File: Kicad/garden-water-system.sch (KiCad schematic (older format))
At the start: 30 parts, among them J1 Conn_01x02, J10 Screw_Terminal_01x05, J11 Conn_01x04, J12 Conn_01x05, J13 Jack-DC, J2 Conn_01x05, J3 Conn_01x03, J4 Conn_01x03, J5 Conn_01x03, J6 Conn_01x03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

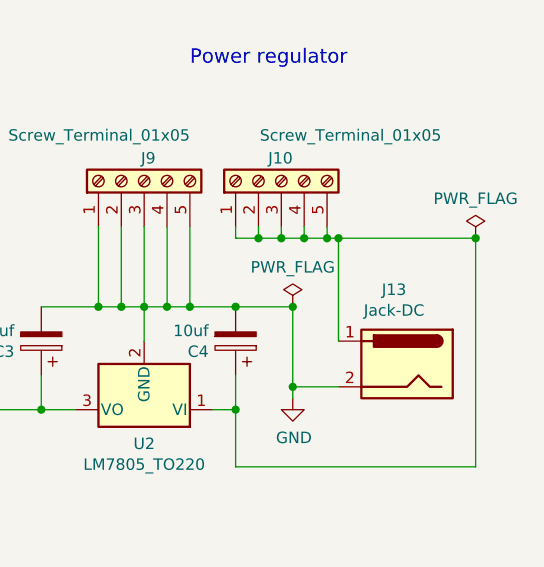
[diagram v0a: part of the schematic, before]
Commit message: Add protection diode on hardware power supply
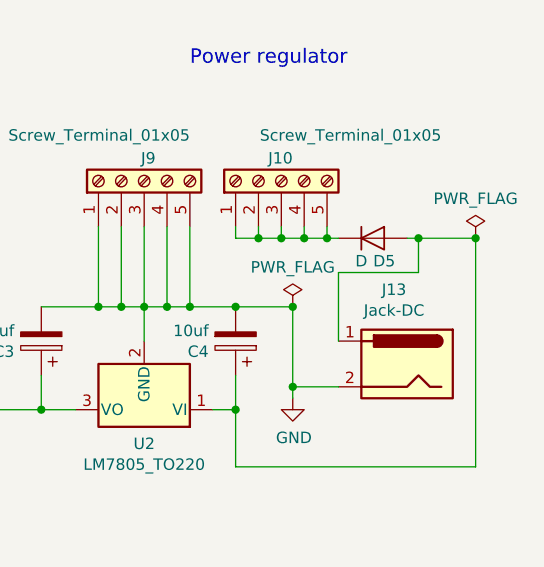
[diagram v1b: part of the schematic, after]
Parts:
- added D5: D, Diode_SMD:D_2010_5025Metric_Pad1.52x2.65mm_HandSolder, symbol Device:D
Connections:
- net at J10.1 (Pin_1), J10.2 (Pin_2), J10.3 (Pin_3)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: now also D5.1 (K); no longer C4.1, J13.1, U2.1 (VI)
- new net: C4.1, D5.2 (A), J13.1, U2.1 (VI)
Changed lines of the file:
@@
 	9400 2250 9400 2100
-Wire Wire Line
-	10200 1800 10250 1800
 Wire Wire Line
 	10850 1800 10850 2800
@@
 	9800 2800 10850 2800
 Wire Wire Line
-	10250 2250 10250 1800
-Connection ~ 10250 1800
-Wire Wire Line
-	10250 1800 10850 1800
+	10200 1800 10250 1800
+$Comp
+L Device:D D5
+U 1 1 5DFEEEC4
+P 10400 1800
+F 0 "D5" H 10450 1700 50  0000 C CNN
+F 1 "D" H 10350 1700 50  0000 C CNN
+F 2 "Diode_SMD:D_2010_5025Metric_Pad1.52x2.65mm_HandSolder" H 10400 1800 50  0001 C CNN
+F 3 "~" H 10400 1800 50  0001 C CNN
+	1    10400 1800
+	1    0    0    -1
+$EndComp
+Wire Wire Line
+	10550 1800 10600 1800
+Wire Wire Line
+	10250 2250 10250 1950
+Wire Wire Line
+	10250 1950 10600 1950
+Wire Wire Line
+	10600 1950 10600 1800
+Connection ~ 10600 1800
+Wire Wire Line
+	10600 1800 10850 1800
 $EndSCHEMATC

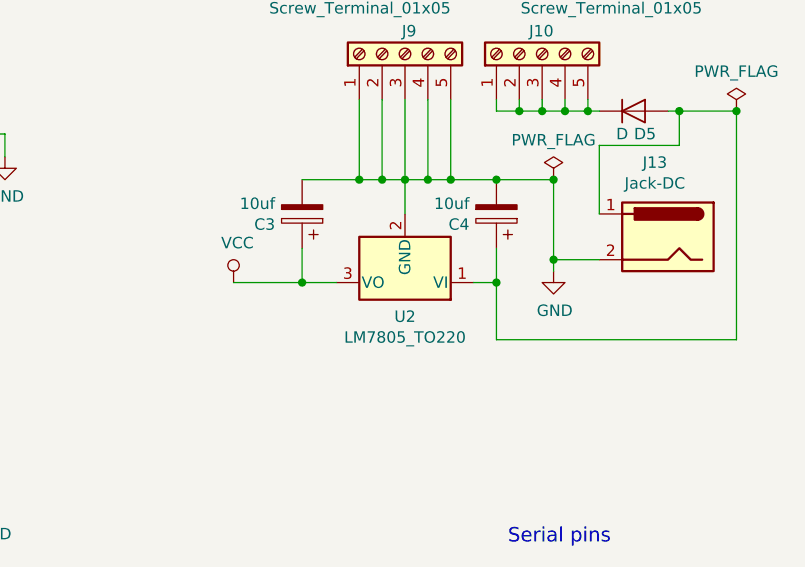
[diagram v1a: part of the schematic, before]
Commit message: Correction pins AMS1117 5.0
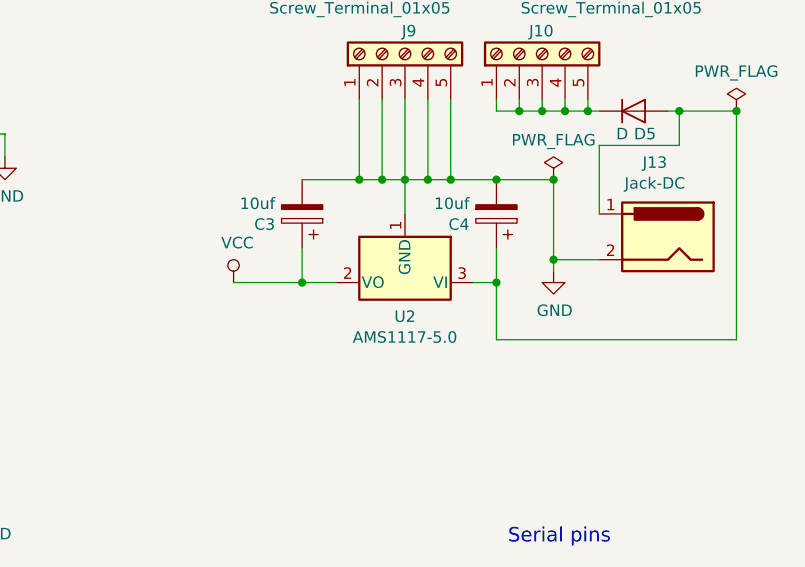
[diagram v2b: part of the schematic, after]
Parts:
- removed U2: LM7805_TO220, Package_TO_SOT_SMD:TO-252-2, symbol Regulator_Linear:LM7805_TO220
- added U2: AMS1117-5.0, Package_TO_SOT_SMD:SOT-223-3_TabPin2, symbol Regulator_Linear:AMS1117-5.0
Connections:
- net GND: now also U2.1 (GND)
- net VCC: now also U2.2 (VO)
- net at C4.1, D5.2 (A), J13.1: now also U2.3 (VI)
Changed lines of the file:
@@
-$EndComp
-$Comp
-L Regulator_Linear:LM7805_TO220 U2
-U 1 1 5DF07E37
-P 9400 2550
-F 0 "U2" H 9400 2699 50  0000 C CNN
-F 1 "LM7805_TO220" H 9400 2790 50  0000 C CNN
-F 2 "Package_TO_SOT_SMD:TO-252-2" H 9400 2775 50  0001 C CIN
-F 3 "http://www.fairchildsemi.com/ds/LM/LM7805.pdf" H 9400 2500 50  0001 C CNN
-	1    9400 2550
-	-1   0    0    1
 $EndComp
 $Comp
@@
 Wire Wire Line
 	10600 1800 10850 1800
+$Comp
+L Regulator_Linear:AMS1117-5.0 U2
+U 1 1 5DFFAF2F
+P 9400 2550
+F 0 "U2" H 9400 2699 50  0000 C CNN
+F 1 "AMS1117-5.0" H 9400 2790 50  0000 C CNN
+F 2 "Package_TO_SOT_SMD:SOT-223-3_TabPin2" H 9400 2750 50  0001 C CNN
+F 3 "http://www.advanced-monolithic.com/pdf/ds1117.pdf" H 9500 2300 50  0001 C CNN
+	1    9400 2550
+	-1   0    0    1
+$EndComp
 $EndSCHEMATC
